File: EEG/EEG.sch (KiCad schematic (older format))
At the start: 48 parts, among them J1 USB_B_Micro, J2 Conn_01x08_Female, J3 Conn_01x08_Female, Q1 2N2219, Q2 2N2219, SW1 SW_Push, SW2 SW_Push, U1 AMS1117-3.3, U2 FT231XS, U3 ESP32-PICO-D4, U4 MAX7219

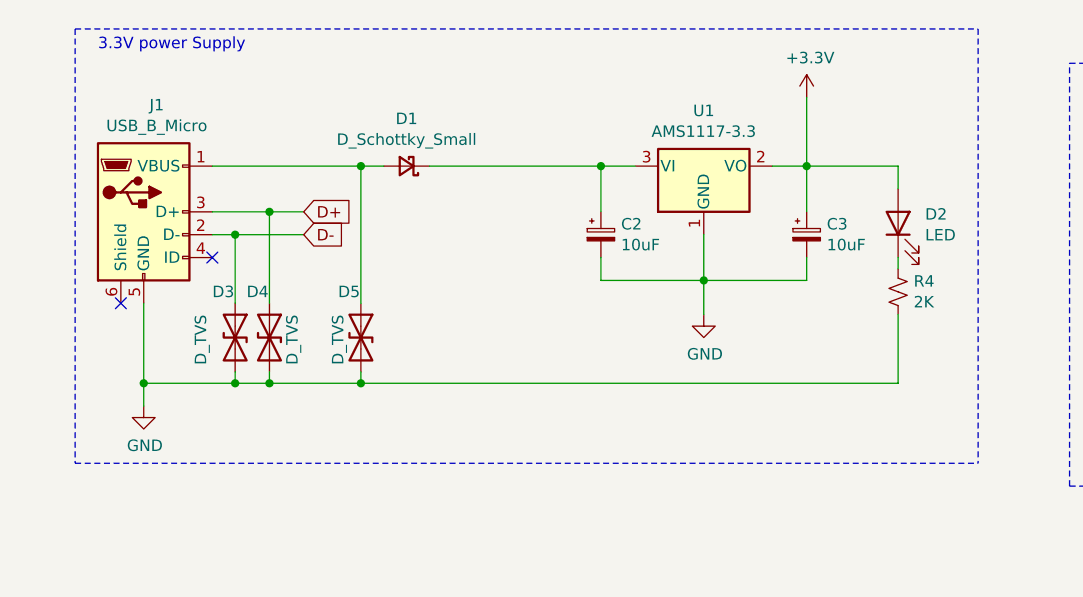
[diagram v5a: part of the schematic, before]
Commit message: need to add max7219 footprint
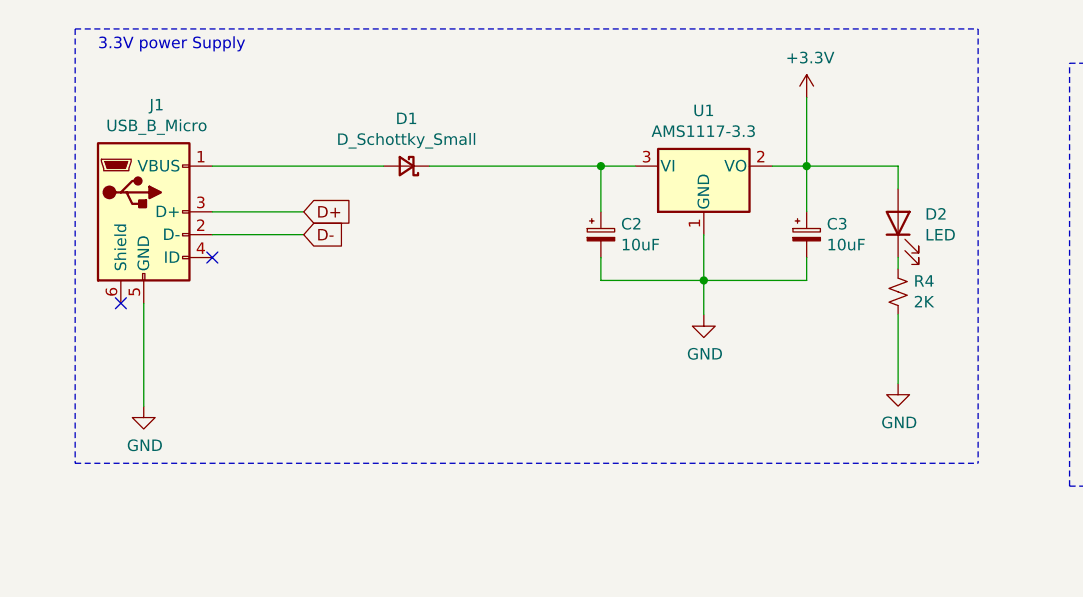
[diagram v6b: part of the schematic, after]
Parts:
- removed D3, D4, D5: D_TVS, symbol Device:D_TVS
- D2: footprint (none) -> LED_SMD:LED_1206_3216Metric_Pad1.42x1.75mm_HandSolder
- J1: footprint (none) -> Connector_USB:USB_Micro-B_Molex-105017-0001
- J2, J3: footprint (none) -> Connector_PinSocket_2.54mm:PinSocket_1x08_P2.54mm_Vertical
- R1, R10, R11, R2, R3, R4, R5, R6, R7, R8, R9: footprint (none) -> Resistor_SMD:R_1206_3216Metric_Pad1.30x1.75mm_HandSolder
- SW1, SW2: footprint (none) -> Button_Switch_SMD:SW_Push_1P1T-SH_NO_CK_KMR2xxG
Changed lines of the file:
@@
 F 0 "J1" H 1357 2067 50  0000 C CNN
 F 1 "USB_B_Micro" H 1357 1976 50  0000 C CNN
-F 2 "" H 1450 1550 50  0001 C CNN
+F 2 "Connector_USB:USB_Micro-B_Molex-105017-0001" H 1450 1550 50  0001 C CNN
 F 3 "~" H 1450 1550 50  0001 C CNN
 	1    1300 1600
@@
 F 0 "R4" H 4668 1996 50  0000 L CNN
 F 1 "2K" H 4668 1905 50  0000 L CNN
-F 2 "" H 4600 1950 50  0001 C CNN
+F 2 "Resistor_SMD:R_1206_3216Metric_Pad1.30x1.75mm_HandSolder" H 4600 1950 50  0001 C CNN
 F 3 "~" H 4600 1950 50  0001 C CNN
 	1    4600 1950
@@
 F 0 "R5" V 10645 2100 50  0000 C CNN
 F 1 "0R" V 10750 2100 50  0000 C CNN
-F 2 "" H 10850 2100 50  0001 C CNN
+F 2 "Resistor_SMD:R_1206_3216Metric_Pad1.30x1.75mm_HandSolder" H 10850 2100 50  0001 C CNN
 F 3 "~" H 10850 2100 50  0001 C CNN
 	1    10850 2100
@@
 F 0 "R6" V 11050 2200 50  0000 C CNN
 F 1 "0R" V 10950 2200 50  0000 C CNN
-F 2 "" H 10850 2200 50  0001 C CNN
+F 2 "Resistor_SMD:R_1206_3216Metric_Pad1.30x1.75mm_HandSolder" H 10850 2200 50  0001 C CNN
 F 3 "~" H 10850 2200 50  0001 C CNN
 	1    10850 2200
@@
 Wire Wire Line
 	11200 2400 11200 2750
-Wire Wire Line
-	1600 1600 1850 1600
-Wire Wire Line
-	1600 1700 1700 1700
-$Comp
-L Device:D_TVS D3
-U 1 1 604B9F05
-P 1700 2150
-F 0 "D3" V 1500 2050 50  0000 L CNN
-F 1 "D_TVS" H 1600 2000 50  0000 L CNN
-F 2 "" H 1700 2150 50  0001 C CNN
-F 3 "~" H 1700 2150 50  0001 C CNN
-	1    1700 2150
-	0    1    1    0
-$EndComp
-$Comp
-L Device:D_TVS D4
-U 1 1 604BADFA
-P 1850 2150
-F 0 "D4" V 1650 2050 50  0000 L CNN
-F 1 "D_TVS" H 1750 2250 50  0000 L CNN
-F 2 "" H 1850 2150 50  0001 C CNN
-F 3 "~" H 1850 2150 50  0001 C CNN
-	1    1850 2150
-	0    1    1    0
-$EndComp
-$Comp
-L Device:D_TVS D5
-U 1 1 604BB310
-P 2250 2150
-F 0 "D5" V 2050 2050 50  0000 L CNN
-F 1 "D_TVS" H 2150 2050 50  0000 L CNN
-F 2 "" H 2250 2150 50  0001 C CNN
-F 3 "~" H 2250 2150 50  0001 C CNN
-	1    2250 2150
-	0    1    1    0
-$EndComp
-Wire Wire Line
-	1300 2000 1300 2350
-Connection ~ 1300 2350
-Wire Wire Line
-	1300 2350 1300 2450
-Wire Wire Line
-	1700 2300 1700 2350
-Connection ~ 1700 2350
-Wire Wire Line
-	1700 2350 1300 2350
-Wire Wire Line
-	1850 2300 1850 2350
-Connection ~ 1850 2350
-Wire Wire Line
-	1850 2350 1700 2350
-Wire Wire Line
-	1700 2000 1700 1700
-Connection ~ 1700 1700
-Wire Wire Line
-	1700 1700 2000 1700
-Wire Wire Line
-	1850 2000 1850 1600
-Connection ~ 1850 1600
-Wire Wire Line
-	1850 1600 2000 1600
 Wire Notes Line
 	1000 800  1000 2700
@@
 F 0 "D2" V 4639 1532 50  0000 R CNN
 F 1 "LED" V 4548 1532 50  0000 R CNN
-F 2 "" H 4600 1650 50  0001 C CNN
+F 2 "LED_SMD:LED_1206_3216Metric_Pad1.42x1.75mm_HandSolder" H 4600 1650 50  0001 C CNN
 F 3 "~" H 4600 1650 50  0001 C CNN
 	1    4600 1650
@@
 F 0 "R7" H 13918 2546 50  0000 L CNN
 F 1 "2K" H 13918 2455 50  0000 L CNN
-F 2 "" H 13850 2500 50  0001 C CNN
+F 2 "Resistor_SMD:R_1206_3216Metric_Pad1.30x1.75mm_HandSolder" H 13850 2500 50  0001 C CNN
 F 3 "~" H 13850 2500 50  0001 C CNN
 	1    13850 2500
@@
 F 0 "SW1" H 6000 1985 50  0000 C CNN
 F 1 "SW_Push" H 6000 1894 50  0000 C CNN
-F 2 "" H 6000 1900 50  0001 C CNN
+F 2 "Button_Switch_SMD:SW_Push_1P1T-SH_NO_CK_KMR2xxG" H 6000 1900 50  0001 C CNN
 F 3 "~" H 6000 1900 50  0001 C CNN
 	1    6000 1700
@@
 F 0 "R1" V 6650 1700 50  0000 C CNN
 F 1 "0R" V 6550 1700 50  0000 C CNN
-F 2 "" H 6450 1700 50  0001 C CNN
+F 2 "Resistor_SMD:R_1206_3216Metric_Pad1.30x1.75mm_HandSolder" H 6450 1700 50  0001 C CNN
 F 3 "~" H 6450 1700 50  0001 C CNN
 	1    6450 1700
@@
 F 0 "SW2" H 8100 1985 50  0000 C CNN
 F 1 "SW_Push" H 8100 1894 50  0000 C CNN
-F 2 "" H 8100 1900 50  0001 C CNN
+F 2 "Button_Switch_SMD:SW_Push_1P1T-SH_NO_CK_KMR2xxG" H 8100 1900 50  0001 C CNN
 F 3 "~" H 8100 1900 50  0001 C CNN
 	1    8100 1700
@@
 F 0 "R2" V 8750 1700 50  0000 C CNN
 F 1 "0R" V 8650 1700 50  0000 C CNN
-F 2 "" H 8550 1700 50  0001 C CNN
+F 2 "Resistor_SMD:R_1206_3216Metric_Pad1.30x1.75mm_HandSolder" H 8550 1700 50  0001 C CNN
 F 3 "~" H 8550 1700 50  0001 C CNN
 	1    8550 1700
@@
 F 0 "R3" H 13918 1746 50  0000 L CNN
 F 1 "2K" H 13918 1655 50  0000 L CNN
-F 2 "" H 13850 1700 50  0001 C CNN
+F 2 "Resistor_SMD:R_1206_3216Metric_Pad1.30x1.75mm_HandSolder" H 13850 1700 50  0001 C CNN
 F 3 "~" H 13850 1700 50  0001 C CNN
 	1    13850 1700
@@
 F 0 "R8" H 6468 4696 50  0000 L CNN
 F 1 "10K" H 6468 4605 50  0000 L CNN
-F 2 "" H 6400 4650 50  0001 C CNN
+F 2 "Resistor_SMD:R_1206_3216Metric_Pad1.30x1.75mm_HandSolder" H 6400 4650 50  0001 C CNN
 F 3 "~" H 6400 4650 50  0001 C CNN
 	1    6400 4650
@@
 F 0 "R9" H 9618 4746 50  0000 L CNN
 F 1 "10K" H 9618 4655 50  0000 L CNN
-F 2 "" H 9550 4700 50  0001 C CNN
+F 2 "Resistor_SMD:R_1206_3216Metric_Pad1.30x1.75mm_HandSolder" H 9550 4700 50  0001 C CNN
 F 3 "~" H 9550 4700 50  0001 C CNN
 	1    9550 4700
@@
 	-1   0    0    1
 $EndComp
-Wire Wire Line
-	1850 2350 2250 2350
-Wire Wire Line
-	2250 2300 2250 2350
-Wire Wire Line
-	2250 2000 2250 1400
-Wire Wire Line
-	1600 1400 2250 1400
-Connection ~ 2250 1400
-Wire Wire Line
-	2250 1400 2350 1400
 $Comp
 L Driver_LED:MAX7219 U4
@@
 F 0 "R10" H 12168 5496 50  0000 L CNN
 F 1 "10k" H 12168 5405 50  0000 L CNN
-F 2 "" H 12100 5450 50  0001 C CNN
+F 2 "Resistor_SMD:R_1206_3216Metric_Pad1.30x1.75mm_HandSolder" H 12100 5450 50  0001 C CNN
 F 3 "~" H 12100 5450 50  0001 C CNN
 	1    12100 5450
@@
 F 0 "R11" H 11668 7396 50  0000 L CNN
 F 1 "10k" H 11668 7305 50  0000 L CNN
-F 2 "" H 11600 7350 50  0001 C CNN
+F 2 "Resistor_SMD:R_1206_3216Metric_Pad1.30x1.75mm_HandSolder" H 11600 7350 50  0001 C CNN
 F 3 "~" H 11600 7350 50  0001 C CNN
 	1    11600 7350
@@
 F 0 "J3" H 3928 9926 50  0000 L CNN
 F 1 "Conn_01x08_Female" H 3928 9835 50  0000 L CNN
-F 2 "" H 3900 9950 50  0001 C CNN
+F 2 "Connector_PinSocket_2.54mm:PinSocket_1x08_P2.54mm_Vertical" H 3900 9950 50  0001 C CNN
 F 3 "~" H 3900 9950 50  0001 C CNN
 	1    3900 9950
@@
 F 0 "J2" H 2228 9826 50  0000 L CNN
 F 1 "Conn_01x08_Female" H 2228 9735 50  0000 L CNN
-F 2 "" H 2200 9850 50  0001 C CNN
+F 2 "Connector_PinSocket_2.54mm:PinSocket_1x08_P2.54mm_Vertical" H 2200 9850 50  0001 C CNN
 F 3 "~" H 2200 9850 50  0001 C CNN
 	1    2200 9850
@@
 	2550 1400 3300 1400
 Wire Wire Line
-	4600 2350 2250 2350
-Wire Wire Line
 	4600 2050 4600 2350
-Connection ~ 2250 2350
 Wire Wire Line
 	4200 1400 4600 1400
@@
 NoConn ~ 7600 5000
 NoConn ~ 13050 7250
+Wire Wire Line
+	1600 1700 2000 1700
+Wire Wire Line
+	1600 1600 2000 1600
+Wire Wire Line
+	1600 1400 2350 1400
+Wire Wire Line
+	1300 2000 1300 2450
+$Comp
+L power:GND #PWR0101
+U 1 1 604B4EB7
+P 4600 2350
+F 0 "#PWR0101" H 4600 2100 50  0001 C CNN
+F 1 "GND" H 4605 2177 50  0000 C CNN
+F 2 "" H 4600 2350 50  0001 C CNN
+F 3 "" H 4600 2350 50  0001 C CNN
+	1    4600 2350
+	1    0    0    -1
+$EndComp
 $EndSCHEMATC

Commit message: ...
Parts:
- U4: footprint (none) -> MAX7219:DIL24
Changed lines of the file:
@@
 F 0 "U4" H 12850 7500 50  0000 C CNN
 F 1 "MAX7219" H 12900 7400 50  0000 C CNN
-F 2 "" H 12600 6500 50  0001 C CNN
+F 2 "MAX7219:DIL24" H 12600 6500 50  0001 C CNN
 F 3 "https://datasheets.maximintegrated.com/en/ds/MAX7219-MAX7221.pdf" H 12700 6300 50  0001 C CNN
 	1    12650 6450
